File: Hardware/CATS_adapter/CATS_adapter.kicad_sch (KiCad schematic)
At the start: 11 parts, among them IC1 LAMBDA80C-24S, J1 Conn_01x04, J2 Conn_02x07_Top_Bottom, SW1 SW_Push, U1 STM32G071CBT6

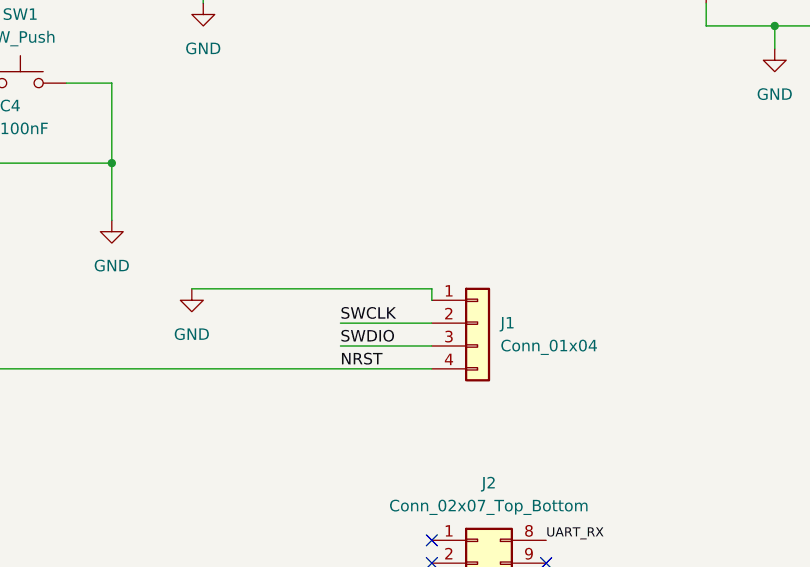
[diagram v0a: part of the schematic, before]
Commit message: CATS changes made: bac keepout zone, 3.3V vref etc..
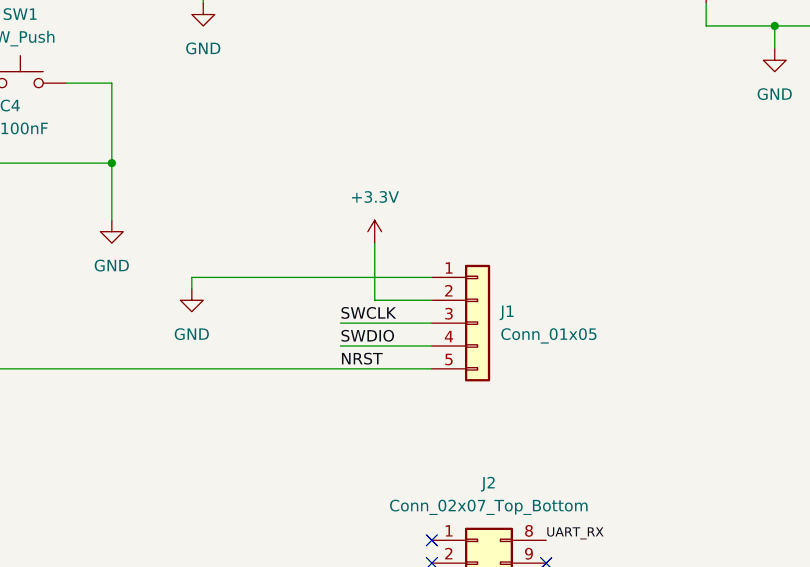
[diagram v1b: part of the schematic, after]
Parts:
- removed J1: Conn_01x04, Connector_PinHeader_2.54mm:PinHeader_1x04_P2.54mm_Vertical, symbol KiCad:Conn_01x04
- added J1: Conn_01x05, Connector_PinHeader_2.54mm:PinHeader_1x05_P2.54mm_Vertical, symbol KiCad:Conn_01x05
- U1: footprint My Feetpics:LQFP-48-L -> Package_QFP:LQFP-48_7x7mm_P0.5mm
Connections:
- net +3.3V: now also J1.2 (Pin_2)
- net GND: now also J1.1 (Pin_1)
- net NRST: now also J1.5 (Pin_5)
- net SWCLK: now also J1.3 (Pin_3)
- net SWDIO: now also J1.4 (Pin_4)
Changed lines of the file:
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@@
+	(wire
+		(pts
+			(xy 158.75 82.55) (xy 165.1 82.55)
+		)
+		(stroke
+			(width 0)
+			(type default)
+		)
+	)
 	(wire
 		(pts
@@
 	(wire
 		(pts
+			(xy 158.75 76.2) (xy 158.75 82.55)
+		)
+		(stroke
+			(width 0)
+			(type default)
+		)
+	)
+	(wire
+		(pts
 			(xy 129.54 58.42) (xy 129.54 67.31)
 		)
@@
 	(wire
 		(pts
-			(xy 165.1 81.28) (xy 165.1 82.55)
+			(xy 138.43 80.01) (xy 165.1 80.01)
 		)
 		(stroke
@@
 	(wire
 		(pts
-			(xy 138.43 81.28) (xy 165.1 81.28)
-		)
-		(stroke
-			(width 0)
-			(type default)
-		)
-	)
-	(wire
-		(pts
 			(xy 185.42 35.56) (xy 189.23 35.56)
 		)
@@
 		(pts
 			(xy 113.03 58.42) (xy 114.3 58.42)
+		)
+		(stroke
+			(width 0)
+			(type default)
+		)
+	)
+	(wire
+		(pts
+			(xy 138.43 81.28) (xy 138.43 80.01)
 		)
 		(stroke
@@
 	)
 	(symbol
-		(lib_id "KiCad:Conn_01x04")
-		(at 170.18 85.09 0)
-		(unit 1)
-		(body_style 1)
-		(exclude_from_sim no)
-		(in_bom yes)
-		(on_board yes)
-		(in_pos_files yes)
-		(dnp no)
-		(fields_autoplaced yes)
-		(property "Reference" "J1"
-			(at 172.72 85.0899 0)
-			(show_name no)
-			(do_not_autoplace no)
-			(effects
-				(font
-					(size 1.27 1.27)
-				)
-				(justify left)
-			)
-		)
-		(property "Value" "Conn_01x04"
-			(at 172.72 87.6299 0)
-			(show_name no)
-			(do_not_autoplace no)
-			(effects
-				(font
-					(size 1.27 1.27)
-				)
-				(justify left)
-			)
-		)
-		(property "Footprint" "Connector_PinHeader_2.54mm:PinHeader_1x04_P2.54mm_Vertical"
-			(at 170.18 85.09 0)
-			(hide yes)
-			(show_name no)
-			(do_not_autoplace no)
-			(effects
-				(font
-					(size 1.27 1.27)
-				)
-			)
-		)
-		(property "Datasheet" ""
-			(at 170.18 85.09 0)
-			(hide yes)
-			(show_name no)
-			(do_not_autoplace no)
-			(effects
-				(font
-					(size 1.27 1.27)
-				)
-			)
-		)
-		(property "Description" "Generic connector, single row, 01x04, script generated (kicad-library-utils/schlib/autogen/connector/)"
-			(at 170.18 85.09 0)
-			(hide yes)
-			(show_name no)
-			(do_not_autoplace no)
-			(effects
-				(font
-					(size 1.27 1.27)
-				)
-			)
-		)
-		(pin "3"
-		)
-		(pin "1"
-		)
-		(pin "2"
-		)
-		(pin "4"
-		)
-		(instances
-			(project "CATS_adapter"
-				(path "/4985fd1e-fa04-47e9-b22a-97ab5736d1c9"
-					(reference "J1")
-					(unit 1)
-				)
-			)
-		)
-	)
-	(symbol
 		(lib_id "KiCad:GND")
 		(at 203.2 54.61 0)
@@
 	)
 	(symbol
+		(lib_id "KiCad:+3.3V")
+		(at 158.75 76.2 0)
+		(unit 1)
+		(body_style 1)
+		(exclude_from_sim no)
+		(in_bom yes)
+		(on_board yes)
+		(in_pos_files yes)
+		(dnp no)
+		(fields_autoplaced yes)
+		(property "Reference" "#PWR014"
+			(at 158.75 80.01 0)
+			(hide yes)
+			(show_name no)
+			(do_not_autoplace no)
+			(effects
+				(font
+					(size 1.27 1.27)
+				)
+			)
+		)
+		(property "Value" "+3.3V"
+			(at 158.75 71.12 0)
+			(show_name no)
+			(do_not_autoplace no)
+			(effects
+				(font
+					(size 1.27 1.27)
+				)
+			)
+		)
+		(property "Footprint" ""
+			(at 158.75 76.2 0)
+			(hide yes)
+			(show_name no)
+			(do_not_autoplace no)
+			(effects
+				(font
+					(size 1.27 1.27)
+				)
+			)
+		)
+		(property "Datasheet" ""
+			(at 158.75 76.2 0)
+			(hide yes)
+			(show_name no)
+			(do_not_autoplace no)
+			(effects
+				(font
+					(size 1.27 1.27)
+				)
+			)
+		)
+		(property "Description" "Power symbol creates a global label with name \"+3.3V\""
+			(at 158.75 76.2 0)
+			(hide yes)
+			(show_name no)
+			(do_not_autoplace no)
+			(effects
+				(font
+					(size 1.27 1.27)
+				)
+			)
+		)
+		(pin "1"
+		)
+		(instances
+			(project "CATS_adapter"
+				(path "/4985fd1e-fa04-47e9-b22a-97ab5736d1c9"
+					(reference "#PWR014")
+					(unit 1)
+				)
+			)
+		)
+	)
+	(symbol
 		(lib_id "KiCad:SW_Push")
 		(at 119.38 58.42 0)
@@
 			)
 		)
-		(property "Footprint" "My Feetpics:LQFP-48-L"
+		(property "Footprint" "Package_QFP:LQFP-48_7x7mm_P0.5mm"
 			(at 30.48 25.4 0)
 			(hide yes)
@@
 	)
 	(symbol
+		(lib_id "KiCad:Conn_01x05")
+		(at 170.18 85.09 0)
+		(unit 1)
+		(body_style 1)
+		(exclude_from_sim no)
+		(in_bom yes)
+		(on_board yes)
+		(in_pos_files yes)
+		(dnp no)
+		(fields_autoplaced yes)
+		(property "Reference" "J1"
+			(at 172.72 83.8199 0)
+			(show_name no)
+			(do_not_autoplace no)
+			(effects
+				(font
+					(size 1.27 1.27)
+				)
+				(justify left)
+			)
+		)
+		(property "Value" "Conn_01x05"
+			(at 172.72 86.3599 0)
+			(show_name no)
+			(do_not_autoplace no)
+			(effects
+				(font
+					(size 1.27 1.27)
+				)
+				(justify left)
+			)
+		)
+		(property "Footprint" "Connector_PinHeader_2.54mm:PinHeader_1x05_P2.54mm_Vertical"
+			(at 170.18 85.09 0)
+			(hide yes)
+			(show_name no)
+			(do_not_autoplace no)
+			(effects
+				(font
+					(size 1.27 1.27)
+				)
+			)
+		)
+		(property "Datasheet" ""
+			(at 170.18 85.09 0)
+			(hide yes)
+			(show_name no)
+			(do_not_autoplace no)
+			(effects
+				(font
+					(size 1.27 1.27)
+				)
+			)
+		)
+		(property "Description" "Generic connector, single row, 01x05, script generated (kicad-library-utils/schlib/autogen/connector/)"
+			(at 170.18 85.09 0)
+			(hide yes)
+			(show_name no)
+			(do_not_autoplace no)
+			(effects
+				(font
+					(size 1.27 1.27)
+				)
+			)
+		)
+		(pin "4"
+		)
+		(pin "2"
+		)
+		(pin "3"
+		)
+		(pin "1"
+		)
+		(pin "5"
+		)
+		(instances
+			(project "CATS_adapter"
+				(path "/4985fd1e-fa04-47e9-b22a-97ab5736d1c9"
+					(reference "J1")
+					(unit 1)
+				)
+			)
+		)
+	)
+	(symbol
 		(lib_id "KiCad:C")
 		(at 113.03 62.23 0)
@@
 			)
 		)
-		(property "Footprint" "My Feetpics:LQFP-48-L"
+		(property "Footprint" "Package_QFP:LQFP-48_7x7mm_P0.5mm"
 			(at 144.78 35.56 0)
 			(hide yes)
